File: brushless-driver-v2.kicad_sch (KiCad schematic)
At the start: 22 parts, among them J1 Conn_01x07_Socket, J2 encoder_r, J5 encoder_l, U1 ESP32-WROOM-32E-R2

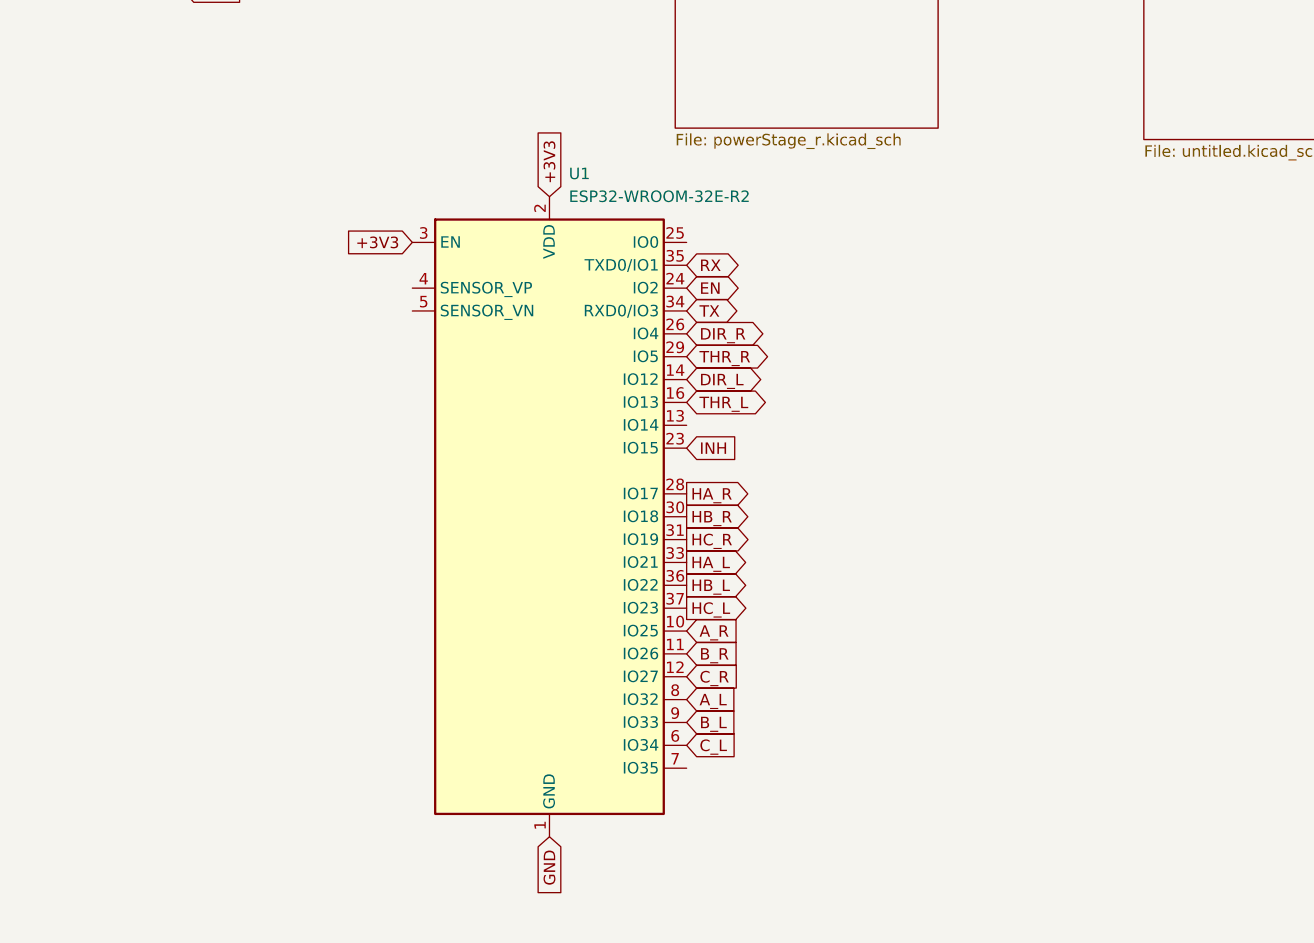
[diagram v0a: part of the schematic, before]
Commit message: added prg port for esp, started on pcb
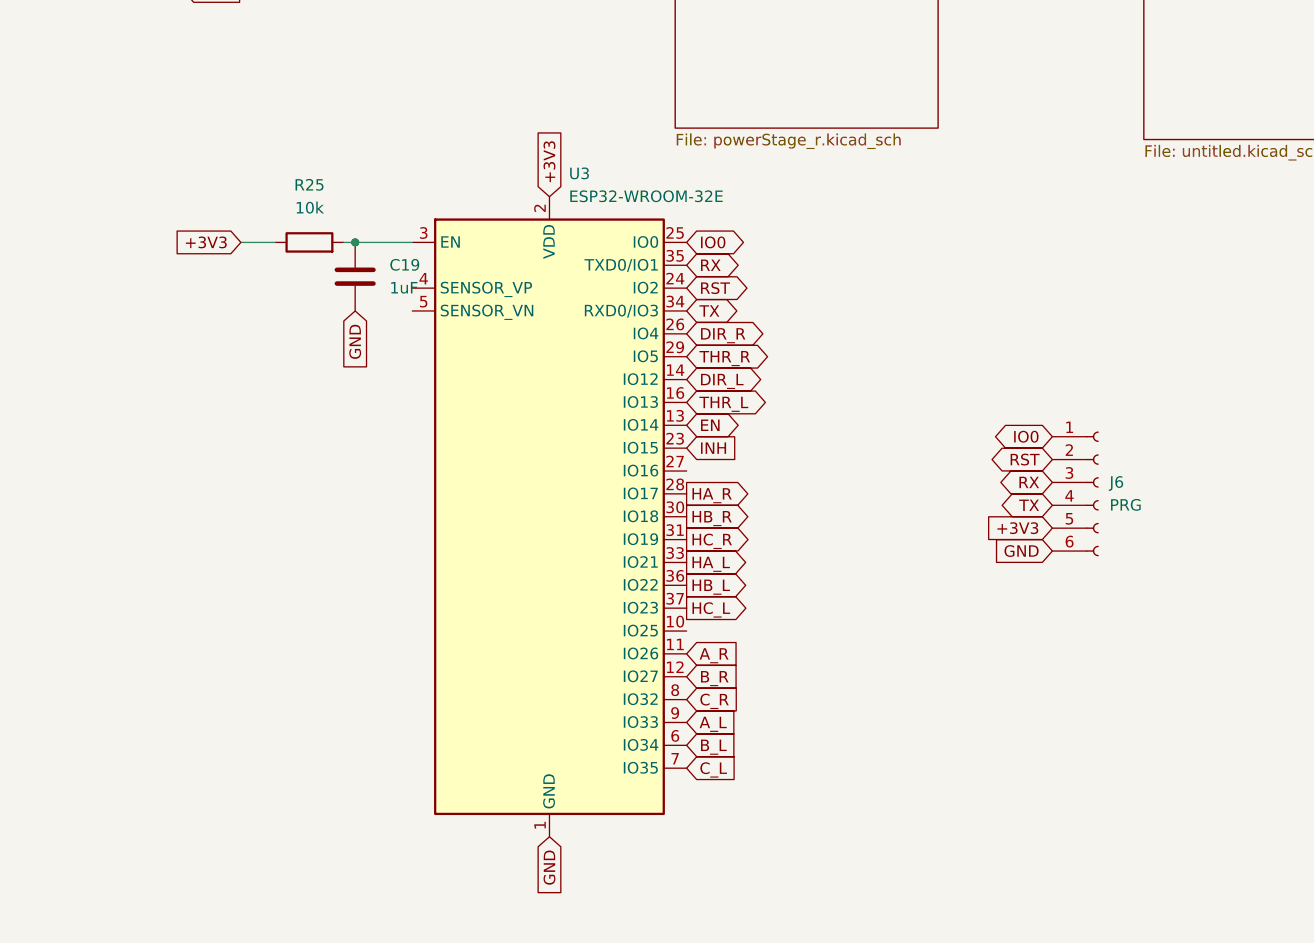
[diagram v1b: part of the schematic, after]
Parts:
- removed U1: ESP32-WROOM-32E-R2, RF_Module:ESP32-WROOM-32D, symbol RF_Module:ESP32-WROOM-32E-R2
- added C19: 1uF, Capacitor_SMD:C_0805_2012Metric_Pad1.18x1.45mm_HandSolder, symbol Device:C
- added J6: PRG, meiBib:Wannenstecker_6pin, symbol Connector:Conn_01x06_Socket
- added R25: 10k, symbol Device:R
- added U3: ESP32-WROOM-32E, RF_Module:ESP32-WROOM-32D, symbol RF_Module:ESP32-WROOM-32E
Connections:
- net +3V3: now also J6.5 (Pin_5), R25.1, U3.2 (VDD)
- net A_L: now also U3.9 (IO33)
- net A_R: now also U3.11 (IO26)
- net B_L: now also U3.6 (IO34)
- net B_R: now also U3.12 (IO27)
- net C_L: now also U3.7 (IO35)
- net C_R: now also U3.8 (IO32)
- net DIR_L: now also U3.14 (IO12)
- net DIR_R: now also U3.26 (IO4)
- net EN: now also U3.13 (IO14)
- net GND: now also C19.2, J6.6 (Pin_6), U3.1 (GND), U3.15 (GND), U3.38 (GND), U3.39 (GND)
- net HA_L: now also U3.33 (IO21)
- net HA_R: now also U3.28 (IO17)
- net HB_L: now also U3.36 (IO22)
- net HB_R: now also U3.30 (IO18)
- net HC_L: now also U3.37 (IO23)
- net HC_R: now also U3.31 (IO19)
- net INH: now also U3.23 (IO15)
- net RX: now also J6.3 (Pin_3), U3.35 (TXD0/IO1)
- net THR_L: now also U3.16 (IO13)
- net THR_R: now also U3.29 (IO5)
- net TX: now also J6.4 (Pin_4), U3.34 (RXD0/IO3)
- new net: C19.1, R25.2, U3.3 (EN)
- new net IO0: J6.1 (Pin_1), U3.25 (IO0)
- new net RST: J6.2 (Pin_2), U3.24 (IO2)

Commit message: still unfinished
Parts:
- removed J1: Conn_01x07_Socket, Connector_JST:JST_PH_S7B-PH-K_1x07_P2.00mm_Horizontal, symbol Connector:Conn_01x07_Socket
- added J7: ext-if, meiBib:Wannenstecker_10pin, symbol Connector:Conn_01x10_Socket
- J6: value PRG -> prg
- R25: footprint (none) -> Resistor_SMD:R_0805_2012Metric_Pad1.20x1.40mm_HandSolder
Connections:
- net +5V: now also J7.2 (Pin_2)
- net A_L: now also U3.31 (IO19); no longer U3.9 (IO33)
- net A_R: now also U3.12 (IO27); no longer U3.11 (IO26)
- net B_L: now also U3.30 (IO18); no longer U3.6 (IO34)
- net B_R: now also U3.11 (IO26); no longer U3.12 (IO27)
- net C_L: now also U3.29 (IO5); no longer U3.7 (IO35)
- net C_R: now also U3.9 (IO33); no longer U3.8 (IO32)
- net DIR_L: now also U3.16 (IO13), J7.8 (Pin_8); no longer U3.14 (IO12)
- net DIR_R: now also J7.6 (Pin_6)
- net EN: now also U3.28 (IO17), J7.5 (Pin_5); no longer U3.13 (IO14)
- net GND: now also J7.1 (Pin_1), J7.10 (Pin_10)
- net HA_R: now also U3.6 (IO34); no longer U3.28 (IO17)
- net HB_R: now also U3.7 (IO35); no longer U3.30 (IO18)
- net HC_R: now also U3.8 (IO32); no longer U3.31 (IO19)
- net RX: now also J7.3 (Pin_3)
- net THR_L: now also U3.14 (IO12), J7.9 (Pin_9); no longer U3.16 (IO13)
- net THR_R: now also U3.27 (IO16), J7.7 (Pin_7); no longer U3.29 (IO5)
- net TX: now also J7.4 (Pin_4)
